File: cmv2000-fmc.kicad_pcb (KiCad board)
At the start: 4 copper layers, 70 x 35 mm, 75 parts, among them J1 Conn_01x02, J10 LVDS_CTR_P, J11 LVDS_CTR_N, J12 LVDS_1_P, J13 LVDS_1_N, J14 LVDS_2_P, J15 LVDS_2_N, J2 Conn_02x05, J3 LVDS_CLK_IN_P, J4 LVDS_CLK_IN_N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

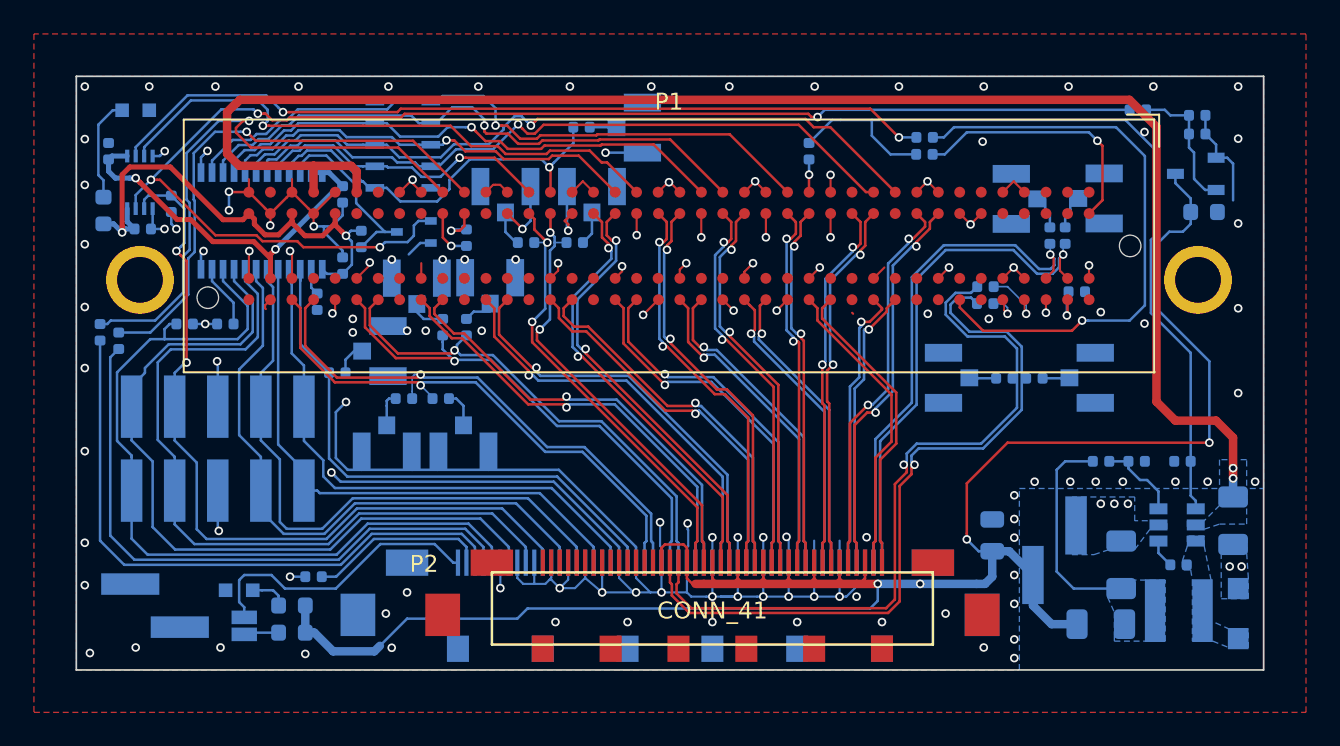
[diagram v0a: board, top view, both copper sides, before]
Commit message: work on layout, change high-frequency resistors to 0201
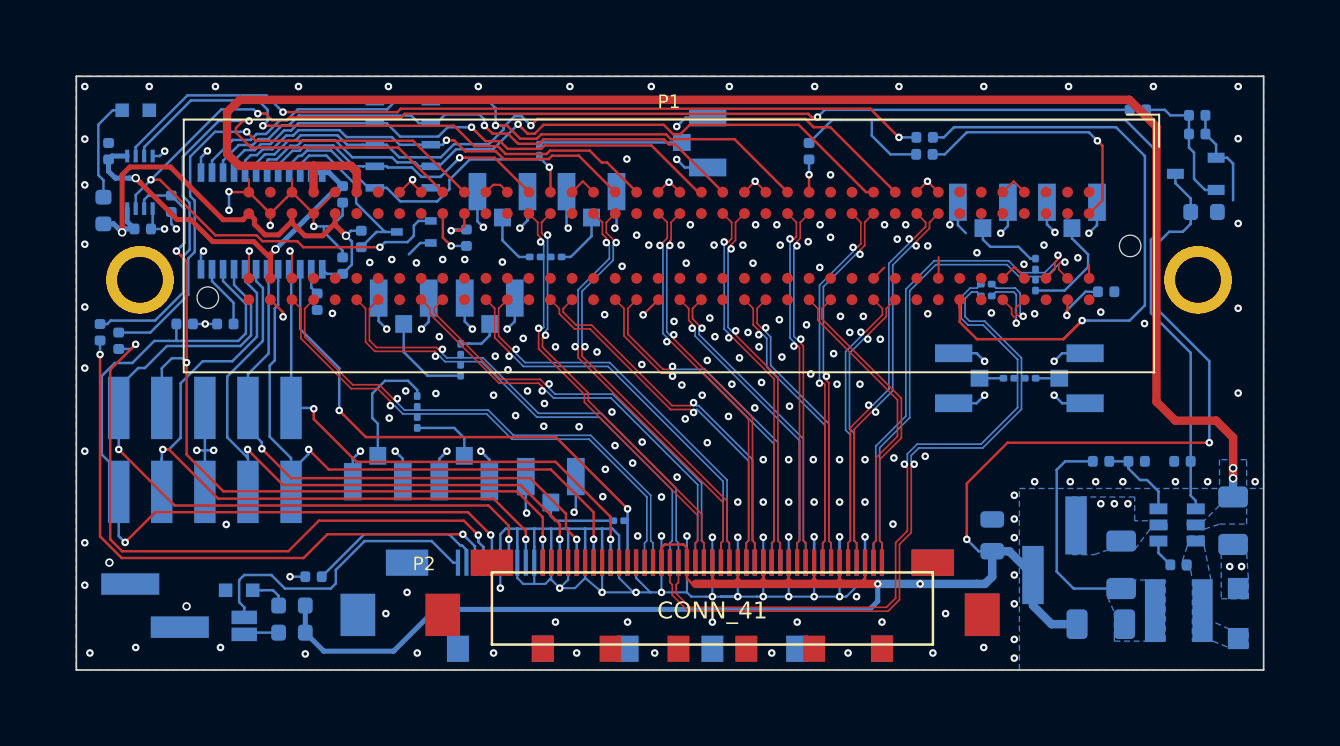
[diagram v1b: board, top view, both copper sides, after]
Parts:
- R15, R16, R17, R20, R23, R24, R25, R26, R30, R31, R32, R33, R34, R35: footprint Resistor_SMD:R_0402_1005Metric -> Resistor_SMD:R_0201_0603Metric
- moved R25 18.7 mm to (144.5, 111.2), turned to 0 degrees
- moved J7 12.8 mm to (140.5, 109.1), turned to 90 degrees
- moved J8 3.95 mm to (149.2, 88.9)
- moved R23 3.40 mm to (169.1, 97.3), turned to 90 degrees
- moved R26 2.83 mm to (139.8, 89.4), turned to 270 degrees
- moved R35 2.75 mm to (135.2, 102.3), turned to 90 degrees
- moved J6 2.25 mm to (165.9, 92.9), turned to 90 degrees
- moved R31 1.98 mm to (132.6, 105.4), turned to 90 degrees
- moved R24 1.88 mm to (169.1, 96.1)
- moved J10 1.87 mm to (130.3, 108.4)
- moved J11 1.80 mm to (135.4, 108.4)
- moved R14 1.73 mm to (173.2, 97.7)
- moved J5 1.59 mm to (171.2, 92.9), turned to 90 degrees
- moved J15 1.41 mm to (131.8, 98.5)
- moved R32 1.39 mm to (140.8, 95.7)
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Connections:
- net Net-(P1-PadH04) renamed /LVDS_CLK_IN_0_P
- net Net-(P1-PadH05) renamed /LVDS_CLK_IN_0_N
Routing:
- net Net-(J8-Pad1): track 1.12 -> 8.46 mm
- net Net-(J10-Pad1): track 1.55 -> 7.33 mm
- net /T_EXP2: track 33.1 -> 38.1 mm, vias 0 -> 2
- net Net-(J5-Pad1): track 1.83 -> 6.37 mm
- net Net-(J15-Pad1): track 1.69 -> 5.59 mm
- net Net-(J7-Pad1): track 1.48 -> 4.99 mm
- net Net-(P1-PadH07): track 35.2 -> 38.0 mm
- net /LVDS_CLK_IN_0_N: track 2.23 -> 5.01 mm
- net /CLK_IN_FMC: track 23.3 -> 20.7 mm
- net Net-(J6-Pad1): track 1.79 -> 4.24 mm
- net Net-(J11-Pad1): track 1.71 -> 4.07 mm
- net /T_EXP1: track 36.3 -> 34.1 mm, vias 0 -> 2
- net /SCL: track 35.9 -> 38.1 mm, vias 0 -> 2
- net Net-(J12-Pad1): track 1.52 -> 3.37 mm
- net /LVDS_CLK_OUT_P: track 30.7 -> 28.9 mm
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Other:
- net class 100R_DIFF added: clearance 0.1, trace_width 0.1, via_dia 0.45, via_drill 0.2
- net class 50R_SE added: clearance 0.1, trace_width 0.146812, via_dia 0.45, via_drill 0.2
- net class DIFF_PAIR removed
- net class Default: via_dia 0.508 -> 0.45; via_drill 0.3048 -> 0.2
- net class Power: via_dia 0.508 -> 0.5; via_drill 0.3048 -> 0.3
- net class PowerSmall: via_dia 0.508 -> 0.5; via_drill 0.3048 -> 0.3
- rule via_min_drill: 0.3 -> 0.2
- rule via_min_size: 0.508 -> 0.45
- board text added: "+"
- board text added: "-"
- board text added: "CAM_PWR"
- board text added: "CLK_IN"
- board text added: "CLK_IN_FMC"
- board text added: "CMV2000 to FMC v0.2 2019-09-15"
- board text added: "FMC_PWR"
- board text added: "GND"
- board text added: "LVDS_1"
- board text added: "LVDS_2"
- board text added: "LVDS_CLK_IN"
- board text added: "LVDS_CLK_OUT"
- board text added: "LVDS_CTR"
- board text added: "N"
- board text added: "P"
- board text added: "V_CAM"
- board text removed: "CMV2000 to FMC v0.2 2018-12-03"

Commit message: slightly increase spacing between pin headers J2 and J9
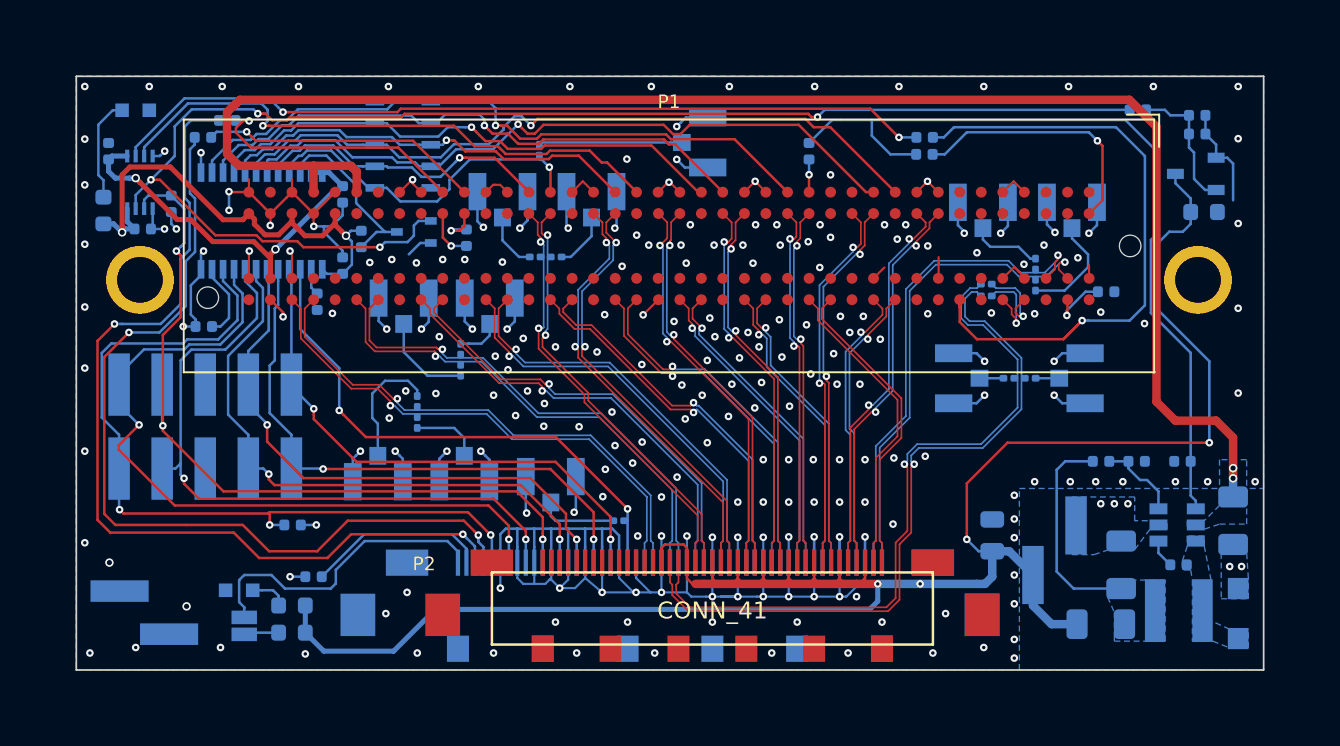
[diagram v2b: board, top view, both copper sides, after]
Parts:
- moved R2 14.6 mm to (121.4, 87.6), turned to 180 degrees
- moved R4 13.5 mm to (125.2, 111.5)
- moved R3 13.0 mm to (120.0, 88.6), turned to 180 degrees
- moved J2 1.38 mm to (120.1, 105.7)
- moved R8 1.28 mm to (120.0, 99.8)
- moved J9 0.75 mm to (116.5, 116.6)
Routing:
- net /SDA: track 36.0 -> 54.3 mm
- net Net-(P1-PadC31): track 33.6 -> 15.7 mm
- net Net-(P1-PadC30): track 31.7 -> 16.5 mm
- net /SCL: track 38.1 -> 51.5 mm
- net GND: track 205.0 -> 202.7 mm, vias 240 -> 237
- net /SYS_RES_N: track 49.8 -> 47.7 mm, vias 2 -> 3
- net /SPI_CLK: track 44.1 -> 45.7 mm
- net /T_EXP1: track 34.1 -> 35.7 mm
- net /SPI_EN: track 44.2 -> 45.3 mm
- net /CAM_PWR_GOOD: track 81.4 -> 82.5 mm
- net /SPI_OUT: track 47.7 -> 46.8 mm
- net Net-(R8-Pad1): track 3.75 -> 4.50 mm
- net /FRAME_REQ: track 32.8 -> 32.1 mm
- net /T_EXP2: track 38.1 -> 37.5 mm
